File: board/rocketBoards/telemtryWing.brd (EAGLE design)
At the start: 160 x 100 mm, 22 parts, among them U3 LS20126

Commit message: telemtry board done
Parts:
- moved C10 107.8 mm to (6.99, 26.7), turned to 90 degrees
- moved C9 104.3 mm to (4.45, 26.7), turned to 90 degrees
- moved C6 100.2 mm to (16.5, 14.6)
- moved C4 99.3 mm to (19.7, 12.7)
- moved C8 98.8 mm to (19.7, 14.6)
- moved C5 91.8 mm to (16.5, 12.7)
- moved R3 87.6 mm to (18.4, 8.89), turned to 180 degrees
- moved R1 82.2 mm to (12.1, 13.3), turned to 180 degrees
- moved C3 80.2 mm to (22.9, 3.81), turned to 90 degrees
- moved LED1 78.4 mm to (8.89, 13.3), turned to 270 degrees
- moved VREG1 77.3 mm to (19.1, 5.08)
- moved R2 77.1 mm to (6.99, 8.89)
- moved JP7 69.4 mm to (15.2, 2.54), turned to 180 degrees
- moved C2 65.2 mm to (8.89, 22.9)
- moved C1 60.2 mm to (8.89, 15.2), turned to 180 degrees
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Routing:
- net GND: track 0.00 -> 141.3 mm, vias 0 -> 1
- net 3.3V: track 0.00 -> 59.1 mm, vias 0 -> 2
- net TXB: track 0.00 -> 35.7 mm, vias 0 -> 3
- net VCC: track 0.00 -> 32.3 mm, vias 0 -> 1
- net GPS_EN: track 0.00 -> 19.7 mm, vias 0 -> 3
- net VBATT: track 0.00 -> 19.6 mm
- net RXB: track 0.00 -> 16.9 mm, vias 0 -> 1
- net I2C_SCL: track 0.00 -> 15.3 mm, vias 0 -> 2
- net TXA: track 0.00 -> 14.1 mm, vias 0 -> 2
- net I2C_SDA: track 0.00 -> 14.1 mm, vias 0 -> 2
- net RXA: track 0.00 -> 11.9 mm, vias 0 -> 2
- net XTAL2: track 0.00 -> 9.79 mm
- net XTAL1: track 0.00 -> 8.95 mm, vias 0 -> 2
- net I2CB2B_SDA: track 0.00 -> 6.23 mm
- net I2CB2B_SCL: track 0.00 -> 5.78 mm
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- added copper zone on layer 1, net GND
- added copper zone on layer 16, net GND
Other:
- board size 160 x 100 mm -> 25.4 x 33 mm

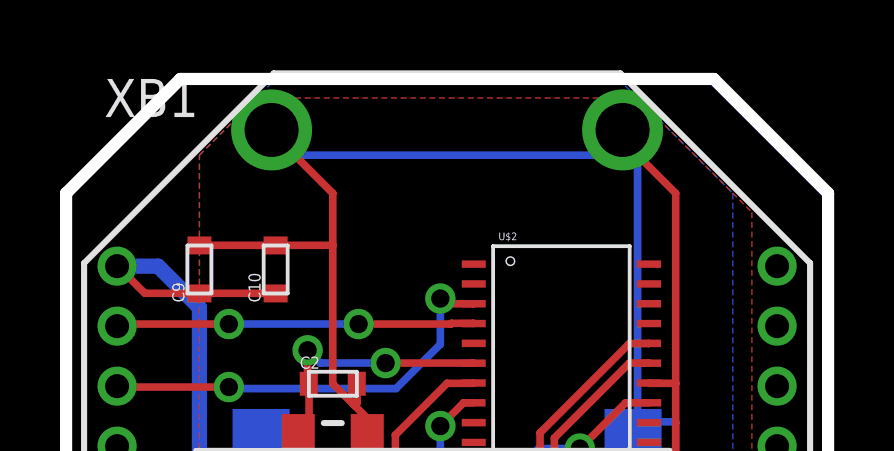
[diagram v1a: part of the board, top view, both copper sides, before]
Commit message: telemtryWing moved board edge down a bit
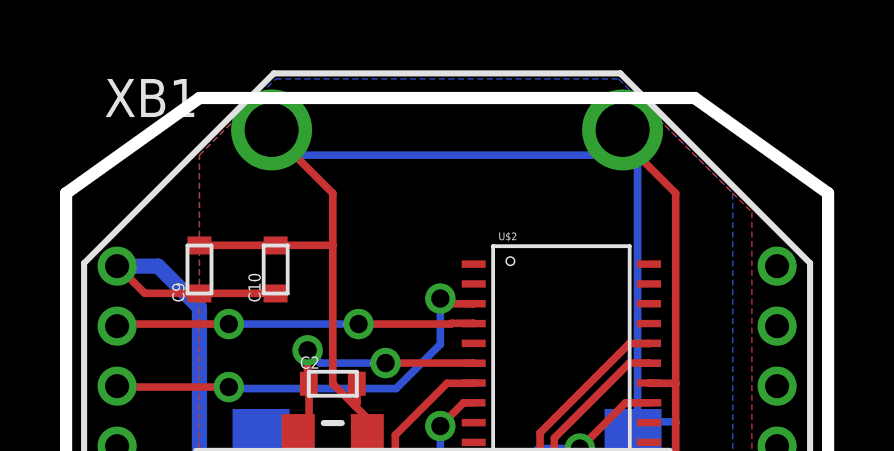
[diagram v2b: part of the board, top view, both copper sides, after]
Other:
- board size 25.4 x 33 mm -> 25.4 x 32.4 mm
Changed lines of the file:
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@@
 <plain>
 <wire x1="0" y1="0" x2="0" y2="29.21" width="0.4064" layer="20"/>
-<wire x1="0" y1="29.21" x2="3.81" y2="33.02" width="0.4064" layer="20"/>
-<wire x1="3.81" y1="33.02" x2="21.59" y2="33.02" width="0.4064" layer="20"/>
-<wire x1="21.59" y1="33.02" x2="25.4" y2="29.21" width="0.4064" layer="20"/>
+<wire x1="0" y1="29.21" x2="4.445" y2="32.385" width="0.4064" layer="20"/>
+<wire x1="4.445" y1="32.385" x2="20.955" y2="32.385" width="0.4064" layer="20"/>
+<wire x1="20.955" y1="32.385" x2="25.4" y2="29.21" width="0.4064" layer="20"/>
 <wire x1="25.4" y1="29.21" x2="25.4" y2="0" width="0.4064" layer="20"/>
 <wire x1="25.4" y1="0" x2="0" y2="0" width="0.4064" layer="20"/>

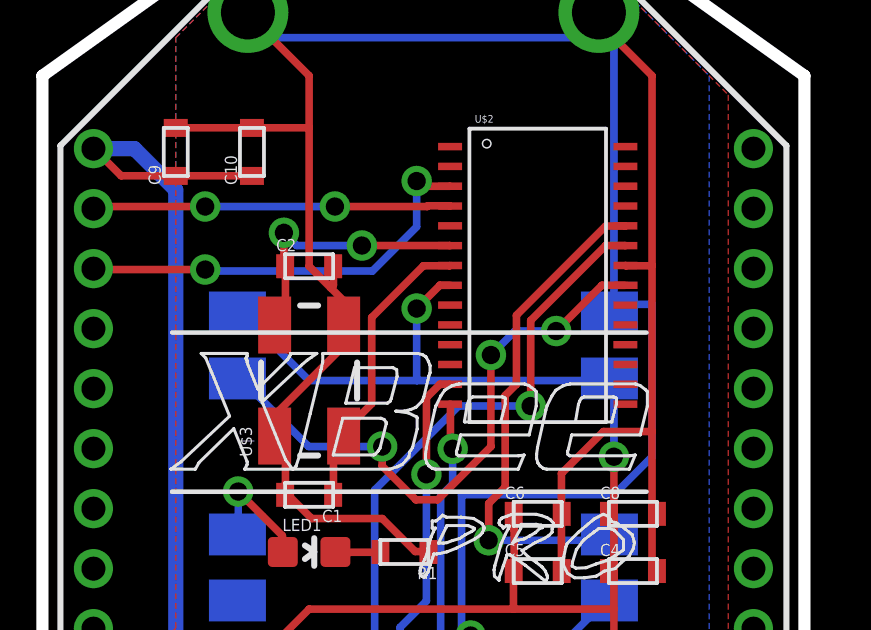
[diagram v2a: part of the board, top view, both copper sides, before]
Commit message: added scienceWing
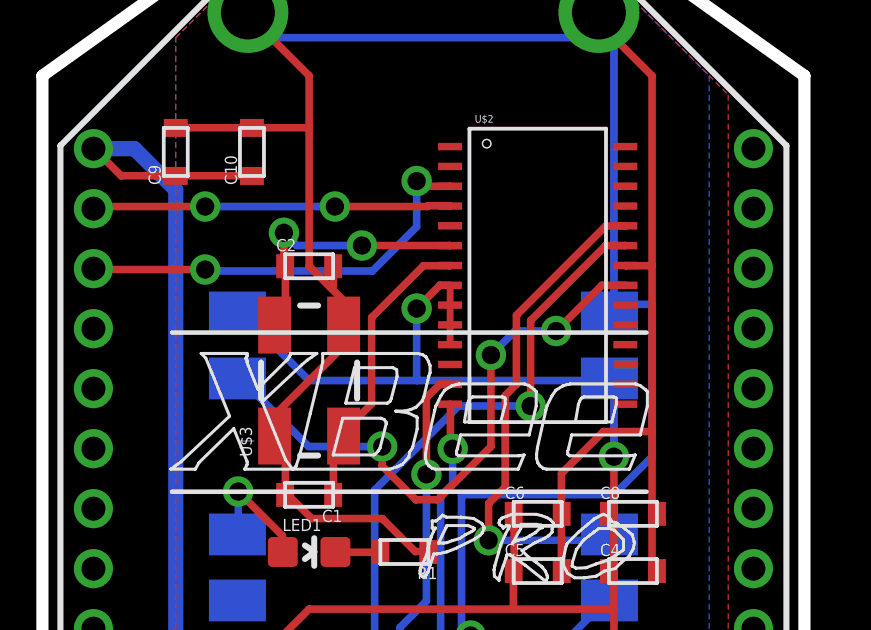
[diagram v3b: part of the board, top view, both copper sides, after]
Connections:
- net 3.3V: now also U$2.10, U$2.11, U$2.9
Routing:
- net 3.3V: track 59.1 -> 61.1 mm
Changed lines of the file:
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@@
 <wire x1="6.4" y1="8.775" x2="6.185" y2="8.89" width="0.254" layer="1"/>
 <via x="12.475" y="21.45" extent="1-16" drill="0.6096"/>
+<contactref element="U$2" pad="9"/>
+<contactref element="U$2" pad="11"/>
+<contactref element="U$2" pad="10"/>
+<wire x1="13.583" y1="22.225" x2="13.589" y2="22.225" width="0.2286" layer="1"/>
+<wire x1="13.589" y1="22.225" x2="13.589" y2="21.5646" width="0.2286" layer="1"/>
+<wire x1="13.589" y1="21.5646" x2="13.589" y2="20.9042" width="0.2286" layer="1"/>
+<wire x1="13.589" y1="20.9042" x2="13.589" y2="20.2438" width="0.2286" layer="1"/>
 </signal>
 <signal name="I2C_SDA">

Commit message: boards shipped
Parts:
- moved U3 6.35 mm to (12.7, 14.0)
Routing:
- net GND: track 141.3 -> 8.68 mm, vias 1 -> 6
- net TXB: track 35.7 -> 10.4 mm, vias 3 -> 1
- net 3.3V: track 61.1 -> 68.5 mm, vias 2 -> 1
- net RXA: track 11.9 -> 18.7 mm, vias 2 -> 0
- net N$3: track 4.08 -> 10.7 mm
- net RXB: track 16.9 -> 10.6 mm
- net GPS_EN: track 19.7 -> 14.3 mm, vias 3 -> 1
- net VCC: track 32.3 -> 30.6 mm
- net I2C_SCL: track 15.3 -> 16.4 mm, vias 2 -> 0
- net TXA: track 14.1 -> 13.0 mm, vias 2 -> 0
- net VBATT: track 19.6 -> 20.5 mm
- net I2CB2B_SCL: track 5.78 -> 6.33 mm
- net I2C_SDA: track 14.1 -> 14.7 mm, vias 2 -> 0
- net XTAL1: track 8.95 -> 9.03 mm, vias 2 -> 0
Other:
- board size 25.4 x 32.4 mm -> 25.4 x 38.7 mm
- board text added: "teamRocket"
- board text added: "telemtryWingV1"
